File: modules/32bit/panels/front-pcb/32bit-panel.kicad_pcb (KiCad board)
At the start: 2 copper layers, 30 x 128.5 mm, 13 parts

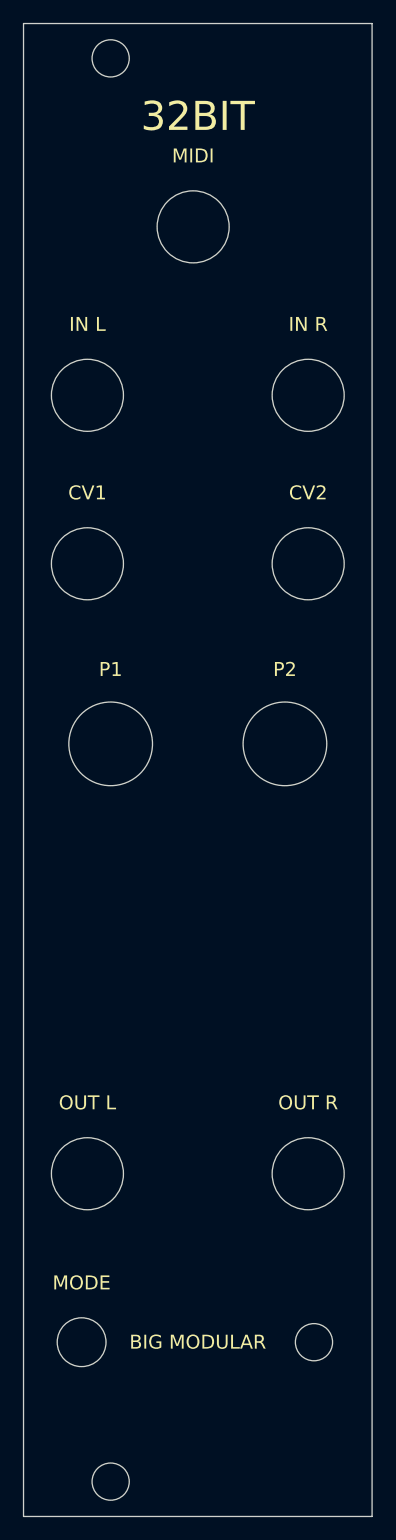
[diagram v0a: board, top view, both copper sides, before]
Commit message: Move panel holes similar to MIDI.
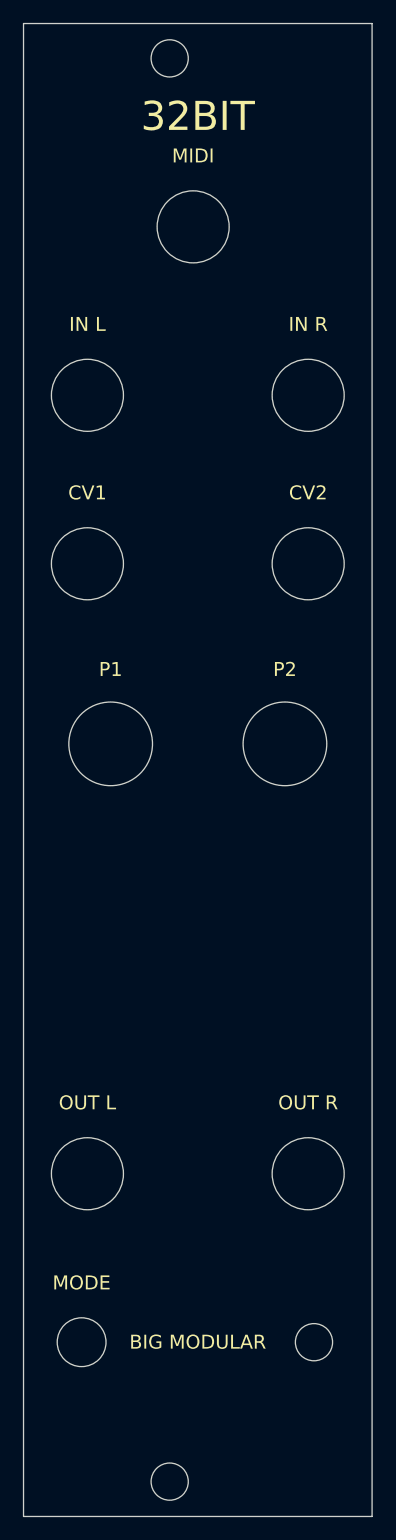
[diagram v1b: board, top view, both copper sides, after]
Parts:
- moved H1 5.08 mm to (112.6, 53.0)
- moved H2 5.08 mm to (112.6, 175.5)
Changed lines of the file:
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@@
 	(footprint ""
 		(layer "F.Cu")
-		(at 107.5 175.5)
+		(at 112.58 175.5)
 		(property "Reference" "H2"
 			(at 0 0 0)
@@
 	(footprint ""
 		(layer "F.Cu")
-		(at 107.5 53)
+		(at 112.58 53)
 		(property "Reference" "H1"
 			(at 0 0 0)
